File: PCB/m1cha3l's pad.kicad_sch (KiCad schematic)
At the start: 11 parts, among them J1 GND-VCC-SCL-SDA, J2 Headers for (Optional) Rotary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, SW1 SW_Push, SW2 SW_Push, SW3 SW_Push, SW4 SW_Push, U1 XIAO-RP2040-DIP

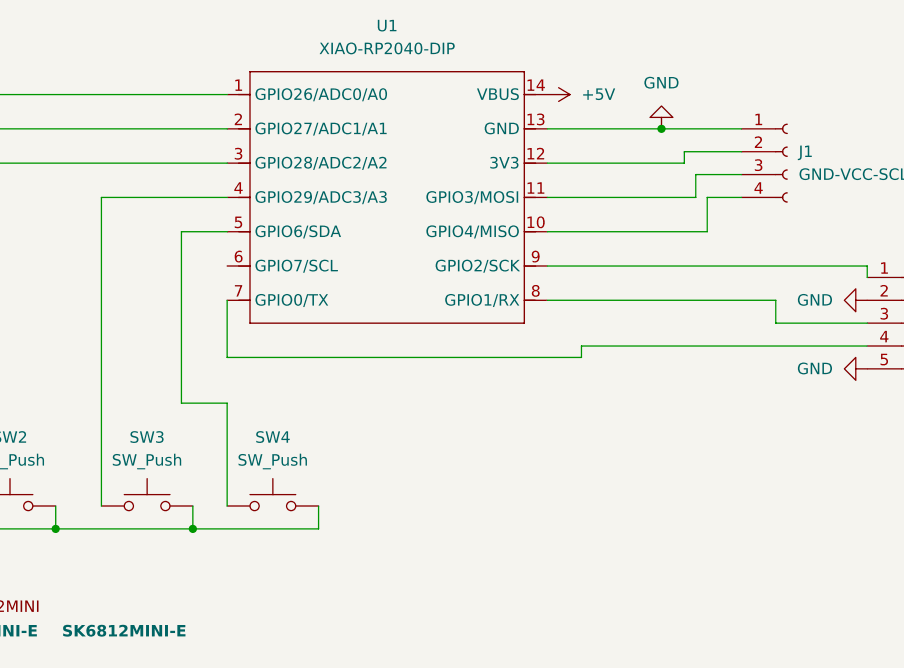
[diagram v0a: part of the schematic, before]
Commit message: Changed SW4 and OLED connection
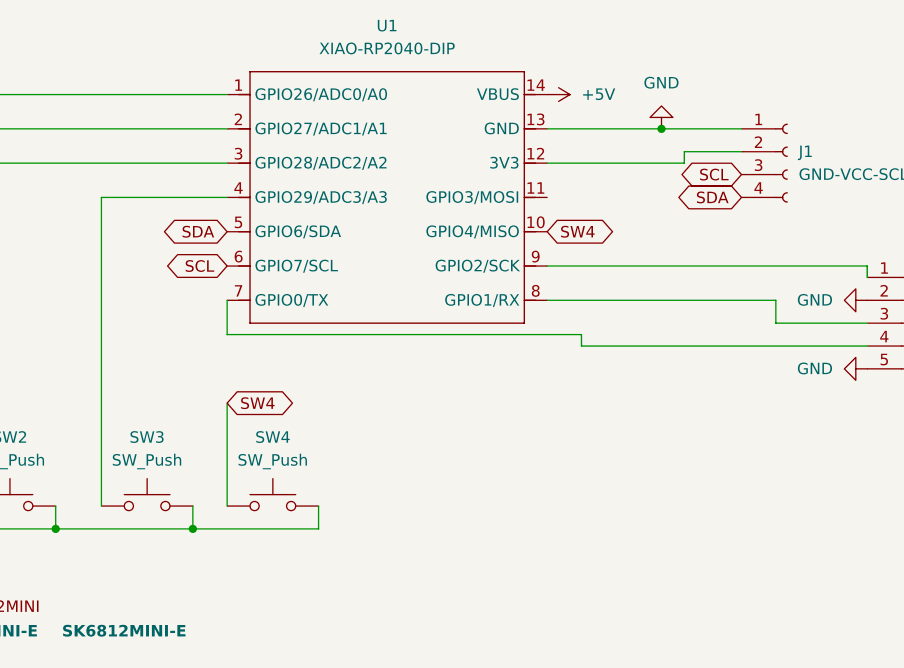
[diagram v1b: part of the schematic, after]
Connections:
- net at U1.11 (GPIO3/MOSI): no longer J1.3 (Pin_3)
- net SDA: now reaches J1.4 (Pin_4)
- net SDA: now also U1.5 (GPIO6/SDA); no longer U1.10 (GPIO4/MISO)
- net SW4: now reaches SW4.1
- net SW4: now also U1.10 (GPIO4/MISO); no longer U1.5 (GPIO6/SDA)
- net SCL: now reaches U1.6 (GPIO7/SCL)
- net SCL: now also J1.3 (Pin_3)
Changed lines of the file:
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@@
 	(wire
 		(pts
-			(xy 181.61 99.06) (xy 198.12 99.06)
-		)
-		(stroke
-			(width 0)
-			(type default)
-		)
-	)
-	(wire
-		(pts
-			(xy 146.05 121.92) (xy 140.97 121.92)
+			(xy 146.05 121.92) (xy 146.05 133.35)
 		)
 		(stroke
@@
 	(wire
 		(pts
-			(xy 198.12 96.52) (xy 203.2 96.52)
-		)
-		(stroke
-			(width 0)
-			(type default)
-		)
-	)
-	(wire
-		(pts
 			(xy 185.42 115.57) (xy 217.17 115.57)
 		)
@@
 	(wire
 		(pts
-			(xy 181.61 102.87) (xy 199.39 102.87)
-		)
-		(stroke
-			(width 0)
-			(type default)
-		)
-	)
-	(wire
-		(pts
 			(xy 58.42 158.75) (xy 64.77 158.75)
 		)
@@
 	(wire
 		(pts
-			(xy 140.97 102.87) (xy 146.05 102.87)
-		)
-		(stroke
-			(width 0)
-			(type default)
-		)
-	)
-	(wire
-		(pts
 			(xy 58.42 143.51) (xy 62.23 143.51)
 		)
@@
 	(wire
 		(pts
-			(xy 185.42 116.84) (xy 185.42 115.57)
+			(xy 146.05 110.49) (xy 146.05 114.3)
+		)
+		(stroke
+			(width 0)
+			(type default)
+		)
+	)
+	(wire
+		(pts
+			(xy 185.42 114.3) (xy 185.42 115.57)
 		)
 		(stroke
@@
 	(wire
 		(pts
-			(xy 140.97 121.92) (xy 140.97 102.87)
-		)
-		(stroke
-			(width 0)
-			(type default)
-		)
-	)
-	(wire
-		(pts
 			(xy 100.33 91.44) (xy 146.05 91.44)
 		)
@@
 	(wire
 		(pts
-			(xy 146.05 133.35) (xy 146.05 121.92)
-		)
-		(stroke
-			(width 0)
-			(type default)
-		)
-	)
-	(wire
-		(pts
 			(xy 207.01 113.03) (xy 217.17 113.03)
 		)
@@
 	(wire
 		(pts
-			(xy 199.39 99.06) (xy 203.2 99.06)
-		)
-		(stroke
-			(width 0)
-			(type default)
-		)
-	)
-	(wire
-		(pts
 			(xy 116.84 95.25) (xy 146.05 95.25)
 		)
@@
 	(wire
 		(pts
-			(xy 146.05 116.84) (xy 146.05 110.49)
-		)
-		(stroke
-			(width 0)
-			(type default)
-		)
-	)
-	(wire
-		(pts
 			(xy 181.61 110.49) (xy 207.01 110.49)
 		)
@@
 	(wire
 		(pts
-			(xy 198.12 99.06) (xy 198.12 96.52)
-		)
-		(stroke
-			(width 0)
-			(type default)
-		)
-	)
-	(wire
-		(pts
 			(xy 196.85 95.25) (xy 196.85 93.98)
 		)
@@
 	(wire
 		(pts
-			(xy 146.05 116.84) (xy 185.42 116.84)
+			(xy 146.05 114.3) (xy 185.42 114.3)
 		)
 		(stroke
@@
 	(wire
 		(pts
-			(xy 199.39 102.87) (xy 199.39 99.06)
-		)
-		(stroke
-			(width 0)
-			(type default)
-		)
-	)
-	(wire
-		(pts
 			(xy 132.08 99.06) (xy 146.05 99.06)
 		)
@@
 		)
 	)
+	(global_label "SCL"
+		(shape bidirectional)
+		(at 146.05 106.68 180)
+		(fields_autoplaced yes)
+		(effects
+			(font
+				(size 1.27 1.27)
+			)
+			(justify right)
+		)
+		(property "Intersheetrefs" "${INTERSHEET_REFS}"
+			(at 138.4459 106.68 0)
+			(effects
+				(font
+					(size 1.27 1.27)
+				)
+				(justify right)
+				(hide yes)
+			)
+		)
+	)
+	(global_label "SDA"
+		(shape bidirectional)
+		(at 203.2 99.06 180)
+		(fields_autoplaced yes)
+		(effects
+			(font
+				(size 1.27 1.27)
+			)
+			(justify right)
+		)
+		(property "Intersheetrefs" "${INTERSHEET_REFS}"
+			(at 195.5354 99.06 0)
+			(effects
+				(font
+					(size 1.27 1.27)
+				)
+				(justify right)
+				(hide yes)
+			)
+		)
+	)
+	(global_label "SW4"
+		(shape bidirectional)
+		(at 181.61 102.87 0)
+		(fields_autoplaced yes)
+		(effects
+			(font
+				(size 1.27 1.27)
+			)
+			(justify left)
+		)
+		(property "Intersheetrefs" "${INTERSHEET_REFS}"
+			(at 189.5769 102.87 0)
+			(effects
+				(font
+					(size 1.27 1.27)
+				)
+				(justify left)
+				(hide yes)
+			)
+		)
+	)
+	(global_label "SCL"
+		(shape bidirectional)
+		(at 203.2 96.52 180)
+		(fields_autoplaced yes)
+		(effects
+			(font
+				(size 1.27 1.27)
+			)
+			(justify right)
+		)
+		(property "Intersheetrefs" "${INTERSHEET_REFS}"
+			(at 195.5959 96.52 0)
+			(effects
+				(font
+					(size 1.27 1.27)
+				)
+				(justify right)
+				(hide yes)
+			)
+		)
+	)
+	(global_label "SDA"
+		(shape bidirectional)
+		(at 146.05 102.87 180)
+		(fields_autoplaced yes)
+		(effects
+			(font
+				(size 1.27 1.27)
+			)
+			(justify right)
+		)
+		(property "Intersheetrefs" "${INTERSHEET_REFS}"
+			(at 138.3854 102.87 0)
+			(effects
+				(font
+					(size 1.27 1.27)
+				)
+				(justify right)
+				(hide yes)
+			)
+		)
+	)
+	(global_label "SW4"
+		(shape bidirectional)
+		(at 146.05 121.92 0)
+		(fields_autoplaced yes)
+		(effects
+			(font
+				(size 1.27 1.27)
+			)
+			(justify left)
+		)
+		(property "Intersheetrefs" "${INTERSHEET_REFS}"
+			(at 154.0169 121.92 0)
+			(effects
+				(font
+					(size 1.27 1.27)
+				)
+				(justify left)
+				(hide yes)
+			)
+		)
+	)
